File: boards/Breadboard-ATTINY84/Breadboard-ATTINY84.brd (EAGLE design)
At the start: 15.2 x 27.9 mm, 10 parts, among them J1 PINHD-1X7, J2 PINHD-1X7, U1 ATTINY84-20PU

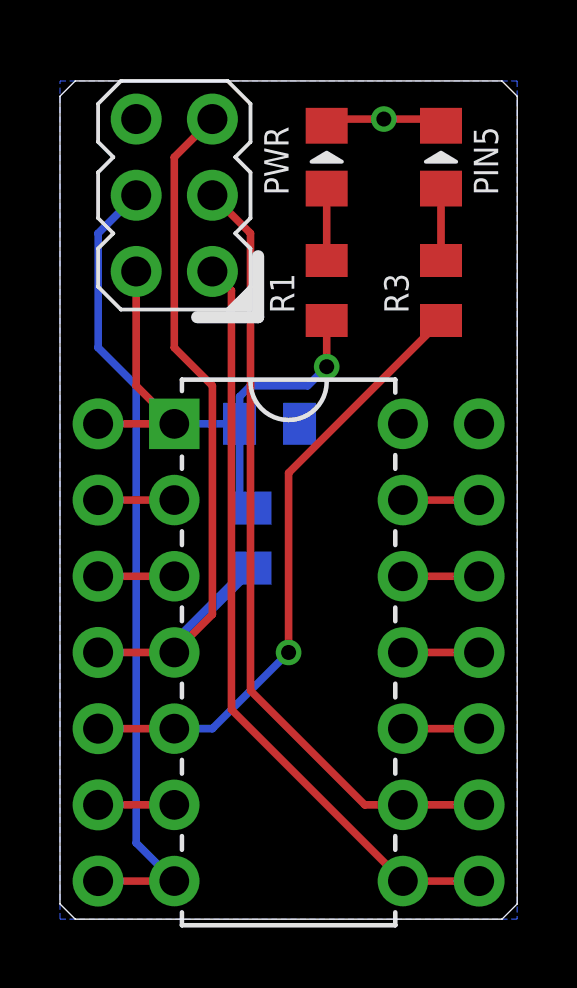
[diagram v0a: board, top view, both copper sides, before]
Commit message: Add a bit of space to breadboard adapters to ICSP connector will fit
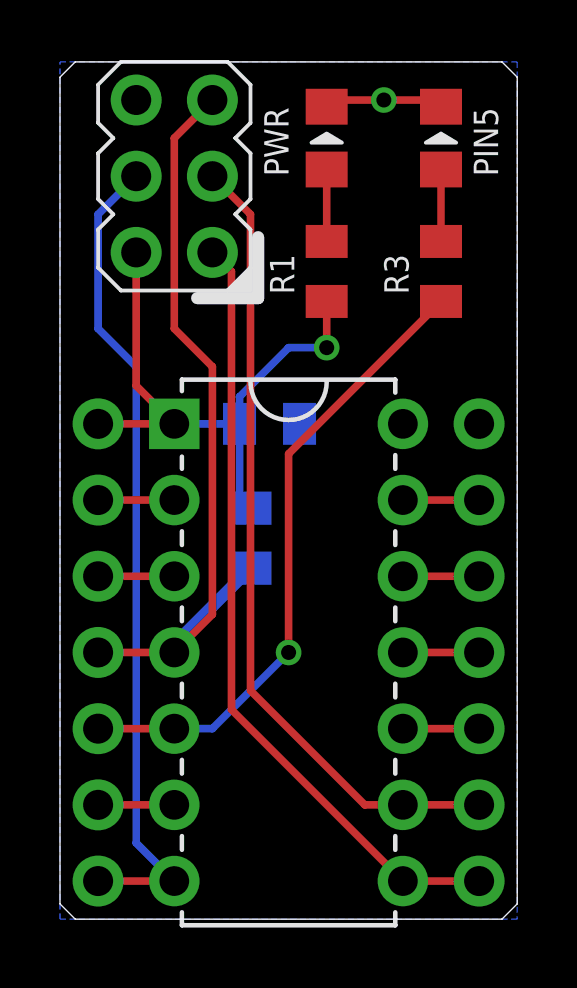
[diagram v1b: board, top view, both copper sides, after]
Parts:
- moved D1 0.64 mm to (8.89, 26.0)
- moved D2 0.64 mm to (12.7, 26.0)
- moved ISP1 0.64 mm to (3.81, 24.8)
- moved R1 0.64 mm to (8.89, 21.6)
- moved R3 0.64 mm to (12.7, 21.6)
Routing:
- net VCC: track 19.0 -> 19.9 mm
- net SCK: track 26.2 -> 26.9 mm
- net MISO: track 25.5 -> 26.1 mm
- net MOSI: track 27.0 -> 27.6 mm
- net LED: track 20.6 -> 21.2 mm
- net RST: track 25.8 -> 26.4 mm
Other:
- board size 15.2 x 27.9 mm -> 15.2 x 28.6 mm
- board text added: "v1.2"
- board text removed: "v1.1"
